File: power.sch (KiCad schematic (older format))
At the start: 36 parts, among them U1 TPS54325, U2 TPS54294

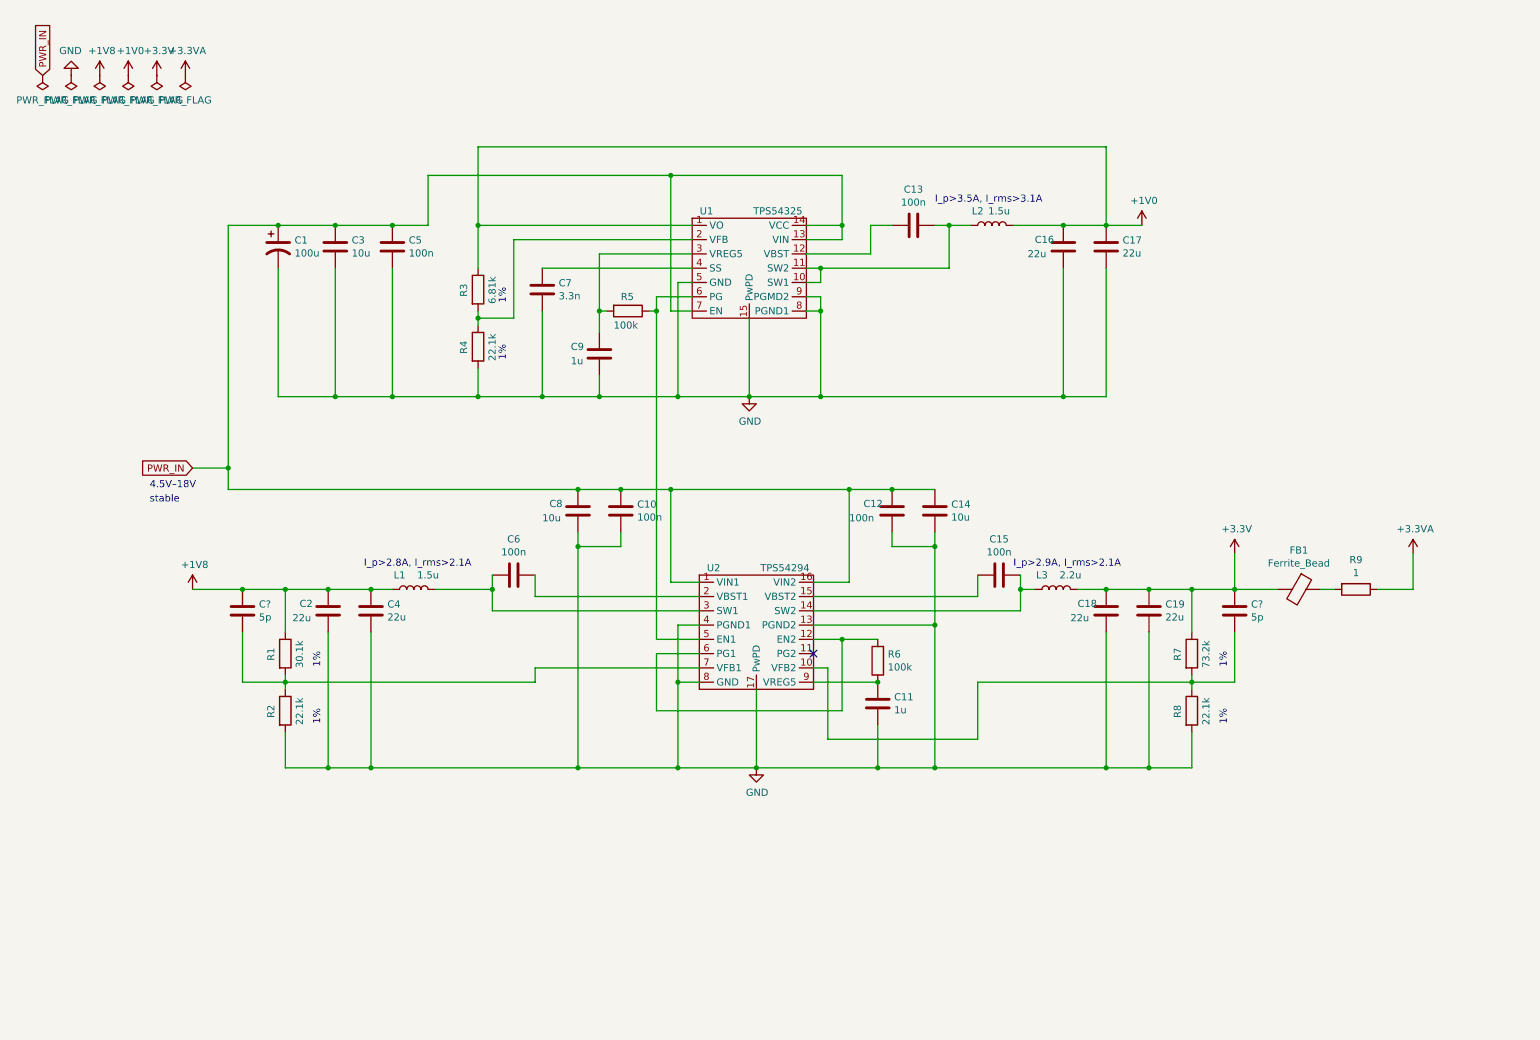
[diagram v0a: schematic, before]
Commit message: Add PSU 5VA and pin headers and change power symbols
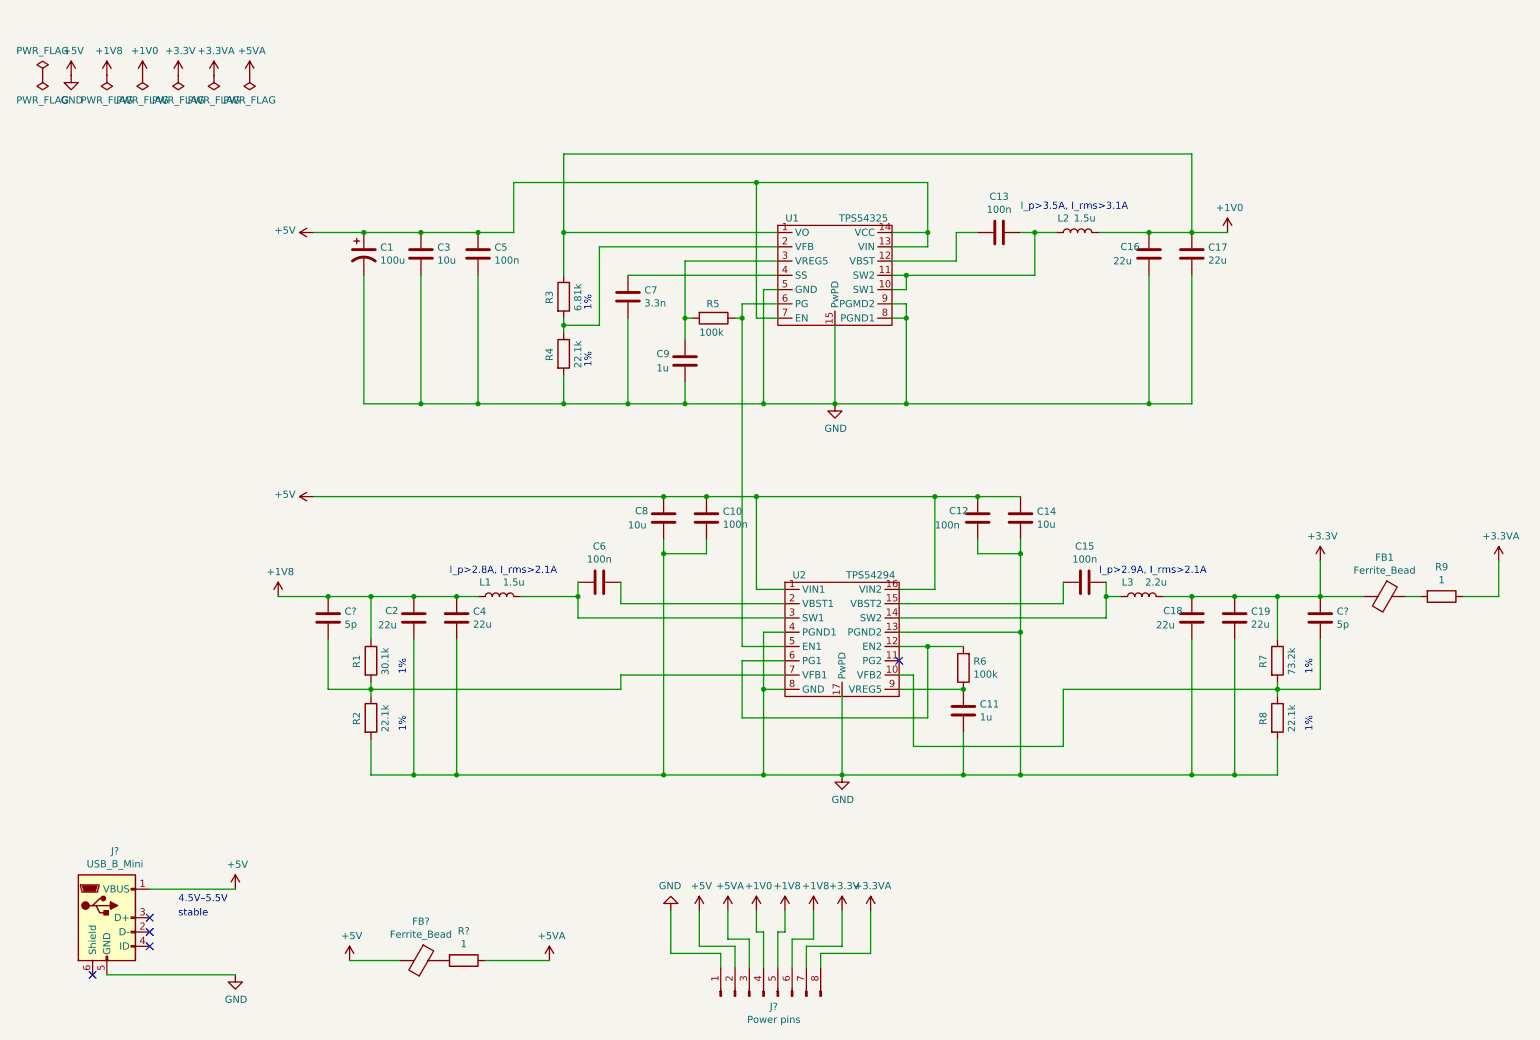
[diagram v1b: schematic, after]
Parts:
- added FB?: Ferrite_Bead, symbol Device:Ferrite_Bead
- added J?: USB_B_Mini, symbol Connector:USB_B_Mini
- added J?: Power pins, symbol Connector:Conn_01x08_Male
- added R?: 1, symbol Device:R
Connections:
- net PWR_IN is gone; now on net +5V: C1.1, C10.1, C12.1, C14.1, C3.1, C5.1, C8.1, U1.13 (VIN), U1.14 (VCC), U1.7 (EN), U2.1 (VIN1), U2.16 (VIN2)
- net +1V0: now also J?.4 (Pin_4)
- net +1V8: now also J?.5 (Pin_5), J?.6 (Pin_6)
- net +3.3VA: now also J?.8 (Pin_8)
- net +3V3: now also J?.7 (Pin_7)
- net GND renamed +5V
- net +5V: now also FB?.2, J?.1 (Pin_1), J?.1 (VBUS), J?.2 (Pin_2), J?.5 (GND)
- new net: FB?.1, R?.2
- new net +5VA: J?.3 (Pin_3), R?.1
- no-connect marks 1 -> 5
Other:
- note added: "4.5V–5.5V"
- note removed: "4.5V–18V"
- moved on the sheet: C1, C10, C11, C12, C13, C14, C15, C16, C17, C18, C19, C2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

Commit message: Add some footprints
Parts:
- J?: footprint (none) -> Local:USB_Mini_B_Female_690-005-299-043
- J?: footprint (none) -> Connector_PinHeader_1.00mm:PinHeader_1x08_P1.00mm_Vertical
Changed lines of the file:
@@
 F 0 "J?" H 1257 7317 50  0000 C CNN
 F 1 "USB_B_Mini" H 1257 7226 50  0000 C CNN
-F 2 "" H 1350 6800 50  0001 C CNN
+F 2 "Local:USB_Mini_B_Female_690-005-299-043" H 1350 6800 50  0001 C CNN
 F 3 "~" H 1350 6800 50  0001 C CNN
 	1    1200 6850
@@
 F 0 "J?" V 5727 7328 50  0000 C CNN
 F 1 "Power pins" V 5636 7328 50  0000 C CNN
-F 2 "" H 5800 7400 50  0001 C CNN
+F 2 "Connector_PinHeader_1.00mm:PinHeader_1x08_P1.00mm_Vertical" V 5545 7328 50  0001 C CNN
 F 3 "~" H 5800 7400 50  0001 C CNN
 	1    5800 7400

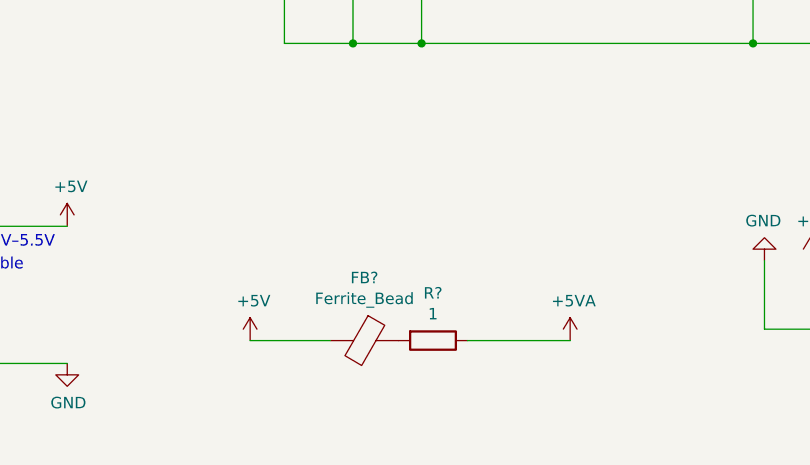
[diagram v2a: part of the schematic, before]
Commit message: Add input capacitor to 5VA
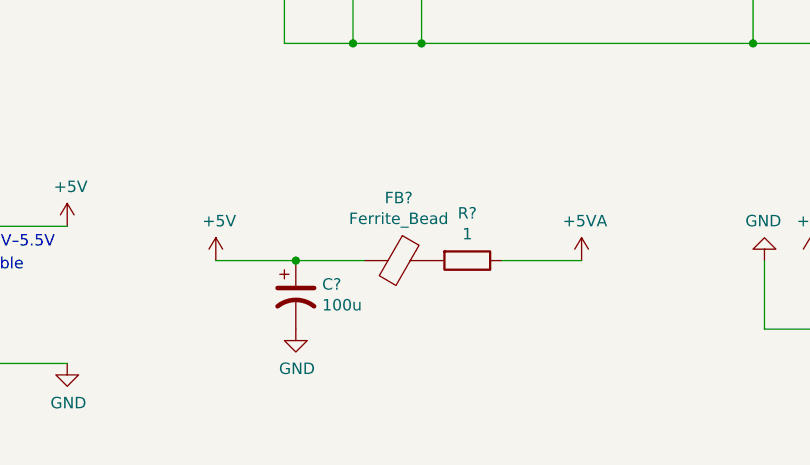
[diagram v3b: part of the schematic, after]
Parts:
- added C?: 100u, symbol Device:CP1
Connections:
- net +5V: now also C?.1, C?.2
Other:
- moved on the sheet: FB?, R?
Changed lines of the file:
@@
 L Device:Ferrite_Bead FB?
 U 1 1 5D9BDE05
-P 3400 7150
-F 0 "FB?" V 3126 7150 50  0000 C CNN
-F 1 "Ferrite_Bead" V 3217 7150 50  0000 C CNN
-F 2 "" V 3330 7150 50  0001 C CNN
-F 3 "~" H 3400 7150 50  0001 C CNN
-	1    3400 7150
+P 3550 6800
+F 0 "FB?" V 3276 6800 50  0000 C CNN
+F 1 "Ferrite_Bead" V 3367 6800 50  0000 C CNN
+F 2 "" V 3480 6800 50  0001 C CNN
+F 3 "~" H 3550 6800 50  0001 C CNN
+	1    3550 6800
 	0    1    1    0
 $EndComp
@@
 L Device:R R?
 U 1 1 5D9C2216
-P 3700 7150
-F 0 "R?" V 3493 7150 50  0000 C CNN
-F 1 "1" V 3584 7150 50  0000 C CNN
-F 2 "" V 3630 7150 50  0001 C CNN
-F 3 "~" H 3700 7150 50  0001 C CNN
-	1    3700 7150
+P 3850 6800
+F 0 "R?" V 3643 6800 50  0000 C CNN
+F 1 "1" V 3734 6800 50  0000 C CNN
+F 2 "" V 3780 6800 50  0001 C CNN
+F 3 "~" H 3850 6800 50  0001 C CNN
+	1    3850 6800
 	0    1    1    0
 $EndComp
-Wire Wire Line
-	2900 7150 3250 7150
 $Comp
 L power:+5VA #PWR?
 U 1 1 5D9DE346
-P 4300 7150
-F 0 "#PWR?" H 4300 7000 50  0001 C CNN
-F 1 "+5VA" H 4315 7323 50  0000 C CNN
-F 2 "" H 4300 7150 50  0001 C CNN
-F 3 "" H 4300 7150 50  0001 C CNN
-	1    4300 7150
+P 4350 6800
+F 0 "#PWR?" H 4350 6650 50  0001 C CNN
+F 1 "+5VA" H 4365 6973 50  0000 C CNN
+F 2 "" H 4350 6800 50  0001 C CNN
+F 3 "" H 4350 6800 50  0001 C CNN
+	1    4350 6800
 	1    0    0    -1
 $EndComp
@@
 L power:+5V #PWR?
 U 1 1 5DC2D89B
-P 2900 7150
-F 0 "#PWR?" H 2900 7000 50  0001 C CNN
-F 1 "+5V" H 2915 7323 50  0000 C CNN
-F 2 "" H 2900 7150 50  0001 C CNN
-F 3 "" H 2900 7150 50  0001 C CNN
-	1    2900 7150
+P 2750 6800
+F 0 "#PWR?" H 2750 6650 50  0001 C CNN
+F 1 "+5V" H 2765 6973 50  0000 C CNN
+F 2 "" H 2750 6800 50  0001 C CNN
+F 3 "" H 2750 6800 50  0001 C CNN
+	1    2750 6800
 	1    0    0    -1
 $EndComp
@@
 	5100 3900 2650 3900
 Connection ~ 5100 3900
-Wire Wire Line
-	3850 7150 4300 7150
+$Comp
+L Device:CP1 C?
+U 1 1 5D926E21
+P 3100 6950
+F 0 "C?" H 3215 6996 50  0000 L CNN
+F 1 "100u" H 3215 6905 50  0000 L CNN
+F 2 "" H 3100 6950 50  0001 C CNN
+F 3 "~" H 3100 6950 50  0001 C CNN
+	1    3100 6950
+	1    0    0    -1
+$EndComp
+Wire Wire Line
+	2750 6800 3100 6800
+Wire Wire Line
+	3100 6800 3400 6800
+Connection ~ 3100 6800
+Wire Wire Line
+	4350 6800 4000 6800
+$Comp
+L power:GND #PWR?
+U 1 1 5D968808
+P 3100 7100
+F 0 "#PWR?" H 3100 6850 50  0001 C CNN
+F 1 "GND" H 3105 6927 50  0000 C CNN
+F 2 "" H 3100 7100 50  0001 C CNN
+F 3 "" H 3100 7100 50  0001 C CNN
+	1    3100 7100
+	1    0    0    -1
+$EndComp
 $EndSCHEMATC

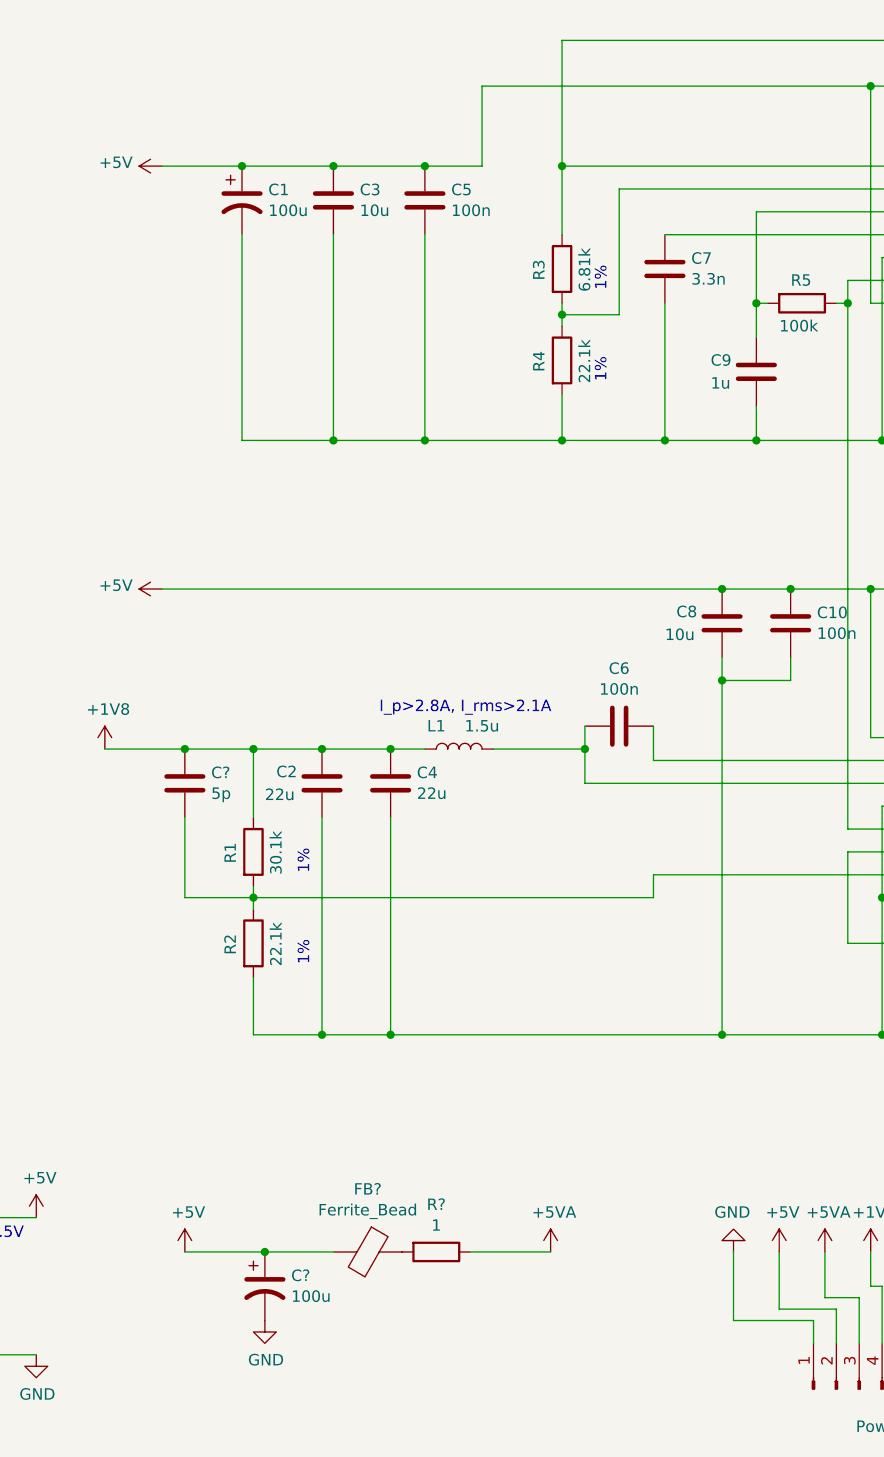
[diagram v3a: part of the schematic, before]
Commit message: Remove extra input capacitors
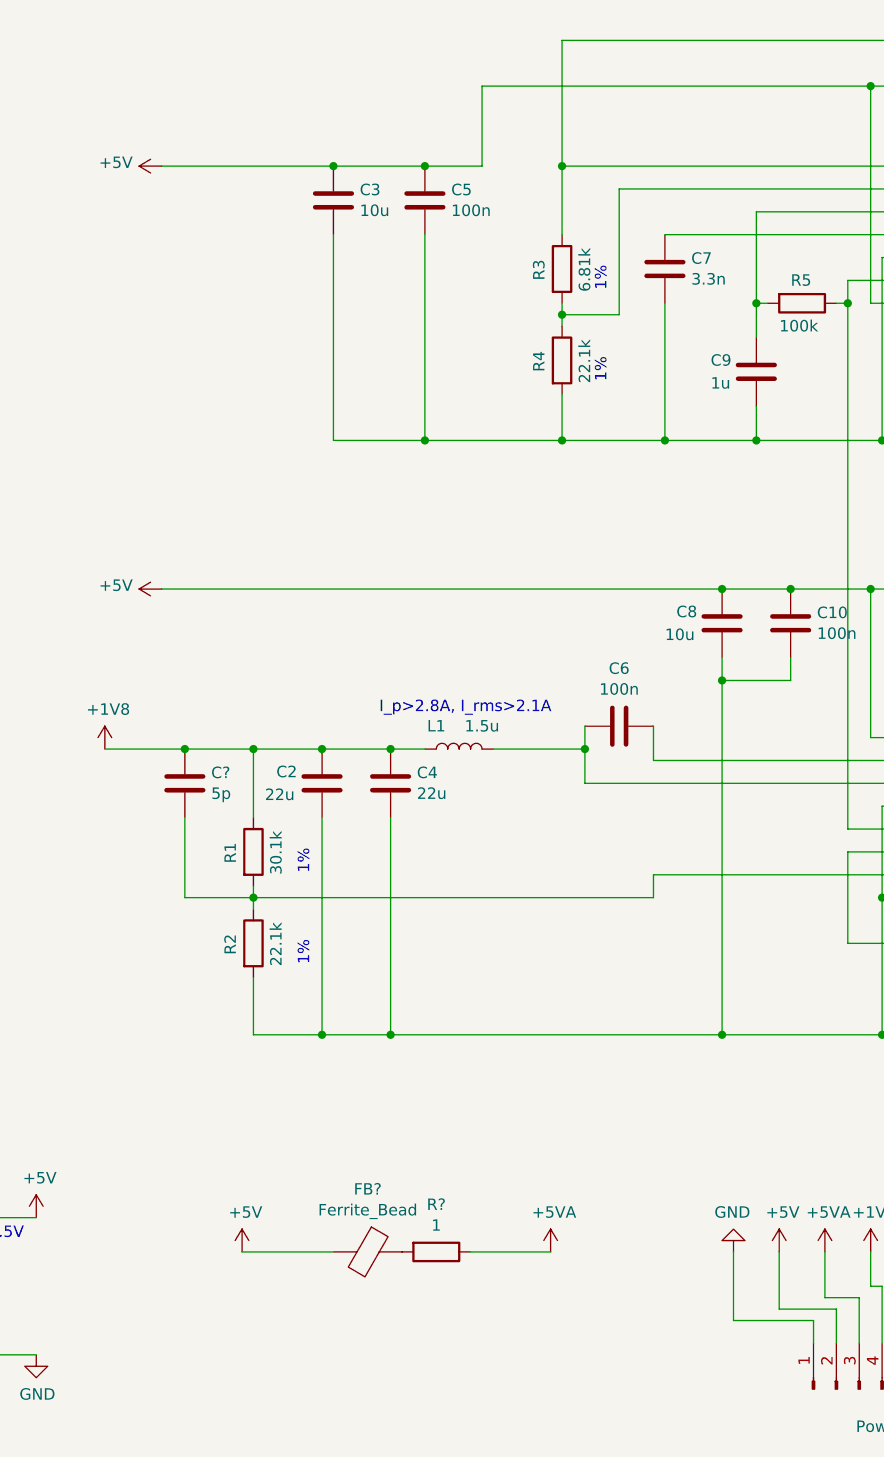
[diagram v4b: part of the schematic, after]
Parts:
- removed C1, C?: 100u, symbol Device:CP1
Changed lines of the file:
@@
 	7000 4550 6750 4550
-Wire Wire Line
-	2650 2050 3000 2050
 Wire Wire Line
 	5750 4550 5950 4550
@@
 Wire Wire Line
 	3800 3250 4400 3250
-Connection ~ 3400 3250
-Wire Wire Line
-	3000 3250 3000 2350
-Wire Wire Line
-	3000 3250 3400 3250
 $Comp
 L Device:C C5
@@
 $EndComp
 Wire Wire Line
-	3000 2050 3400 2050
-Wire Wire Line
 	3400 2350 3400 3250
 Wire Wire Line
 	3400 2050 3800 2050
 Connection ~ 3400 2050
-Connection ~ 3000 2050
-$Comp
-L Device:CP1 C1
-U 1 1 5D868CF6
-P 3000 2200
-F 0 "C1" H 3115 2246 50  0000 L CNN
-F 1 "100u" H 3115 2155 50  0000 L CNN
-F 2 "" H 3000 2200 50  0001 C CNN
-F 3 "~" H 3000 2200 50  0001 C CNN
-	1    3000 2200
-	1    0    0    -1
-$EndComp
 $Comp
 L Device:C C3
@@
 L power:+5V #PWR?
 U 1 1 5DC2D89B
-P 2750 6800
-F 0 "#PWR?" H 2750 6650 50  0001 C CNN
-F 1 "+5V" H 2765 6973 50  0000 C CNN
-F 2 "" H 2750 6800 50  0001 C CNN
-F 3 "" H 2750 6800 50  0001 C CNN
-	1    2750 6800
+P 3000 6800
+F 0 "#PWR?" H 3000 6650 50  0001 C CNN
+F 1 "+5V" H 3015 6973 50  0000 C CNN
+F 2 "" H 3000 6800 50  0001 C CNN
+F 3 "" H 3000 6800 50  0001 C CNN
+	1    3000 6800
 	1    0    0    -1
 $EndComp
@@
 	0    -1   -1   0
 $EndComp
-Wire Wire Line
-	5100 3900 2650 3900
 Connection ~ 5100 3900
-$Comp
-L Device:CP1 C?
-U 1 1 5D926E21
-P 3100 6950
-F 0 "C?" H 3215 6996 50  0000 L CNN
-F 1 "100u" H 3215 6905 50  0000 L CNN
-F 2 "" H 3100 6950 50  0001 C CNN
-F 3 "~" H 3100 6950 50  0001 C CNN
-	1    3100 6950
-	1    0    0    -1
-$EndComp
-Wire Wire Line
-	2750 6800 3100 6800
-Wire Wire Line
-	3100 6800 3400 6800
-Connection ~ 3100 6800
 Wire Wire Line
 	4350 6800 4000 6800
-$Comp
-L power:GND #PWR?
-U 1 1 5D968808
-P 3100 7100
-F 0 "#PWR?" H 3100 6850 50  0001 C CNN
-F 1 "GND" H 3105 6927 50  0000 C CNN
-F 2 "" H 3100 7100 50  0001 C CNN
-F 3 "" H 3100 7100 50  0001 C CNN
-	1    3100 7100
-	1    0    0    -1
-$EndComp
+Wire Wire Line
+	2650 3900 5100 3900
+Wire Wire Line
+	2650 2050 3400 2050
+Wire Wire Line
+	3400 6800 3000 6800
 $EndSCHEMATC

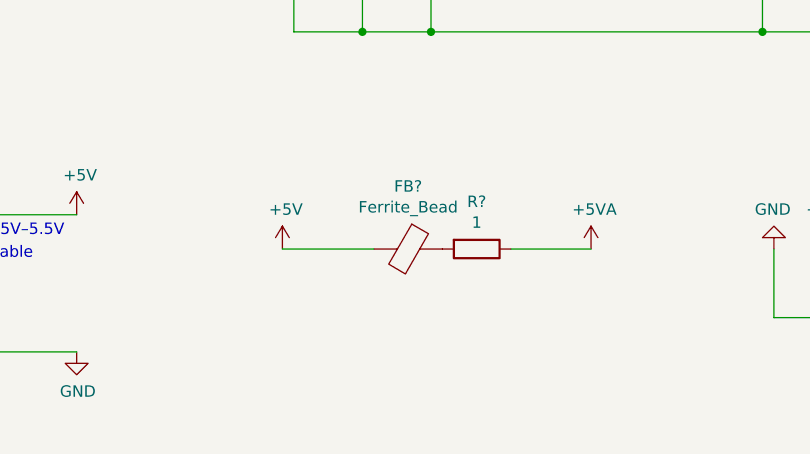
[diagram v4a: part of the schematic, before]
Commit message: Re-add required cap for 5VA
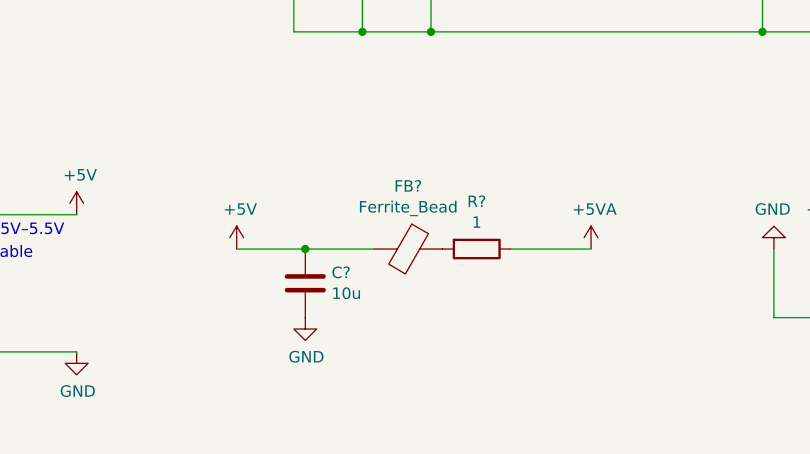
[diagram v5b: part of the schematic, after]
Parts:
- added C?: 10u, symbol Device:C
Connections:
- net +5V: now also C?.1, C?.2
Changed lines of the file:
@@
 L power:+5V #PWR?
 U 1 1 5DC2D89B
-P 3000 6800
-F 0 "#PWR?" H 3000 6650 50  0001 C CNN
-F 1 "+5V" H 3015 6973 50  0000 C CNN
-F 2 "" H 3000 6800 50  0001 C CNN
-F 3 "" H 3000 6800 50  0001 C CNN
-	1    3000 6800
+P 2800 6800
+F 0 "#PWR?" H 2800 6650 50  0001 C CNN
+F 1 "+5V" H 2815 6973 50  0000 C CNN
+F 2 "" H 2800 6800 50  0001 C CNN
+F 3 "" H 2800 6800 50  0001 C CNN
+	1    2800 6800
 	1    0    0    -1
 $EndComp
@@
 Connection ~ 5100 3900
 Wire Wire Line
-	4350 6800 4000 6800
-Wire Wire Line
 	2650 3900 5100 3900
 Wire Wire Line
 	2650 2050 3400 2050
+$Comp
+L Device:C C?
+U 1 1 5D9CD979
+P 3100 6950
+F 0 "C?" H 3215 6996 50  0000 L CNN
+F 1 "10u" H 3215 6905 50  0000 L CNN
+F 2 "" H 3138 6800 50  0001 C CNN
+F 3 "~" H 3100 6950 50  0001 C CNN
+	1    3100 6950
+	1    0    0    -1
+$EndComp
 Wire Wire Line
-	3400 6800 3000 6800
+	2800 6800 3100 6800
+Wire Wire Line
+	3100 6800 3400 6800
+Connection ~ 3100 6800
+Wire Wire Line
+	4000 6800 4350 6800
+$Comp
+L power:GND #PWR?
+U 1 1 5DA02E7A
+P 3100 7100
+F 0 "#PWR?" H 3100 6850 50  0001 C CNN
+F 1 "GND" H 3105 6927 50  0000 C CNN
+F 2 "" H 3100 7100 50  0001 C CNN
+F 3 "" H 3100 7100 50  0001 C CNN
+	1    3100 7100
+	1    0    0    -1
+$EndComp
 $EndSCHEMATC
